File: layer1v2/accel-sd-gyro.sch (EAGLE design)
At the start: 17 parts, among them IC2 LGD20H, U1 MMA8452Q, U2 microSD

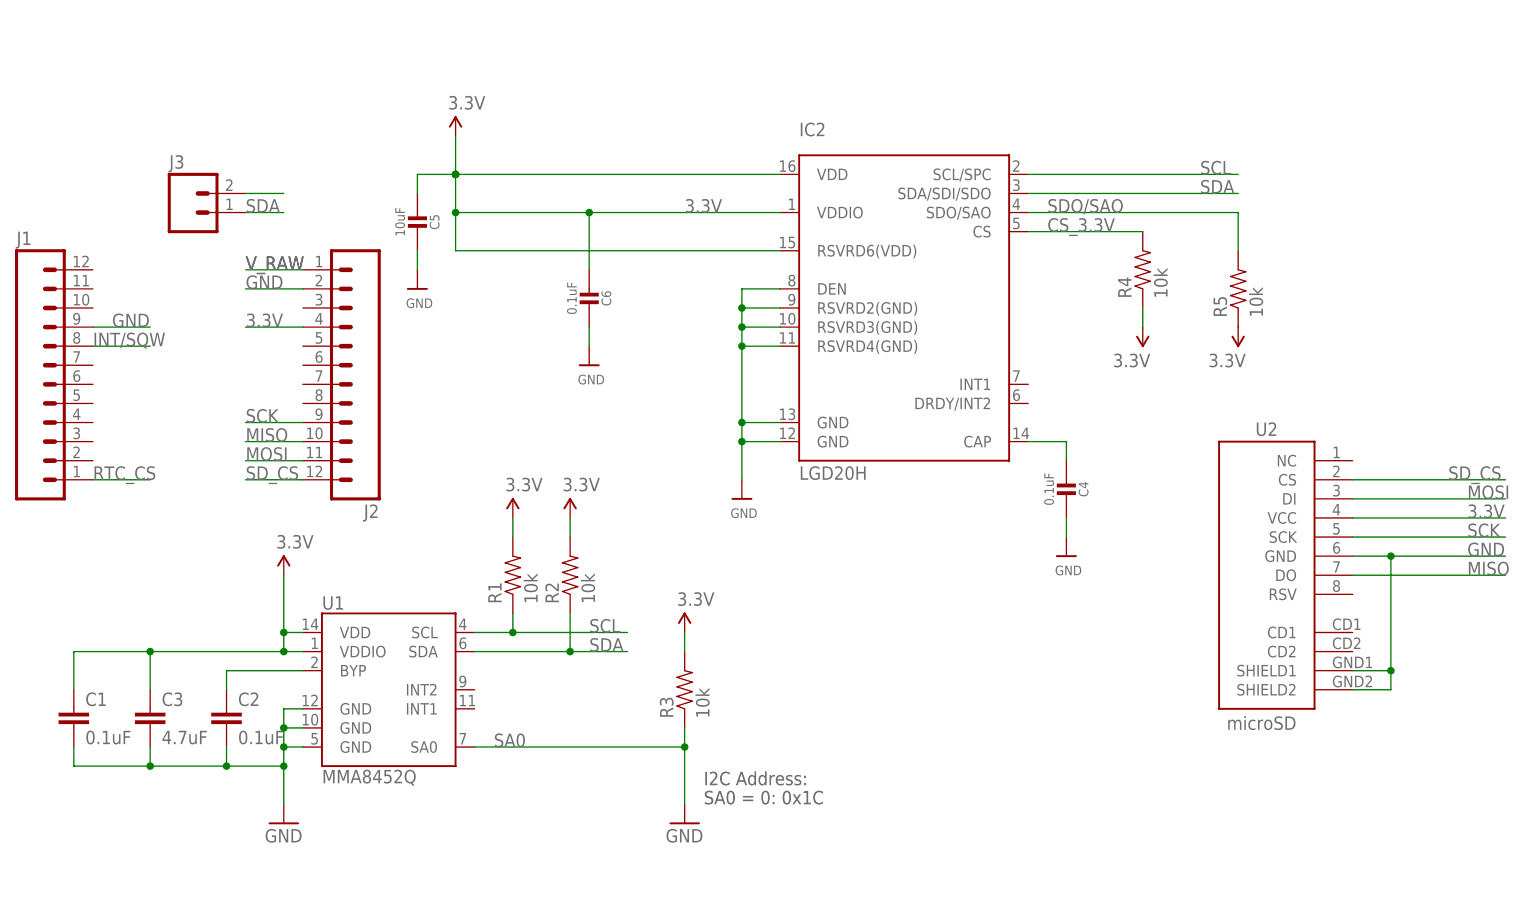
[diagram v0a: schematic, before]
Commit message: intial layout of v2 board, consldated i2c resisor, added header pin row
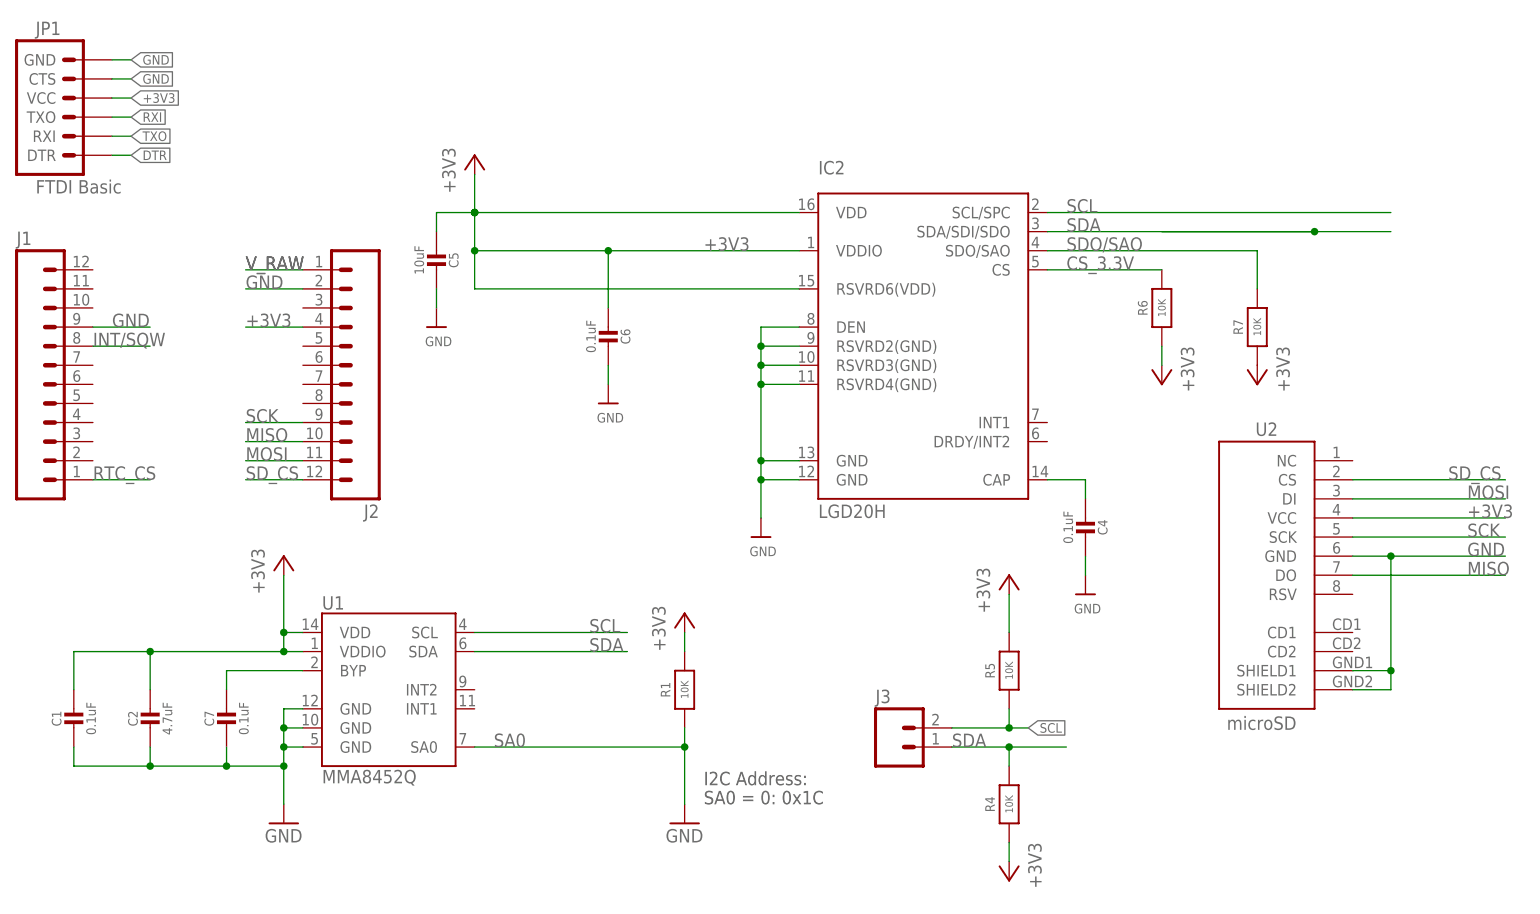
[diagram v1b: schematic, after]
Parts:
- removed C3: 4.7uF, SparkFun:CAP0402-CAP
- removed R2, R3: 10k, SparkFun:RESISTOR0402-RES
- added C7: 0.1uF, microbuilder:CAP_CERAMIC0805-NOOUTLINE
- added JP1: FTDI Basic, SparkFun:ARDUINO_SERIAL_PROGRAMPTH
- added R6: 10K, microbuilder:RESISTOR_0805MP
- added R7: 10K, microbuilder:RESISTOR0805_NOOUTLINE
- C1: device SparkFun:CAP0402-CAP -> microbuilder:CAP_CERAMIC0805-NOOUTLINE
- C2: value 0.1uF -> 4.7uF; device SparkFun:CAP0402-CAP -> microbuilder:CAP_CERAMIC0805-NOOUTLINE
- R1: value 10k -> 10K; device SparkFun:RESISTOR0402-RES -> microbuilder:RESISTOR_0805MP
- R4, R5: value 10k -> 10K; device SparkFun:RESISTOR0402-RES -> microbuilder:RESISTOR0805_NOOUTLINE
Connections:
- removed net 3.3V: C1.1, C3.1, C5.2, C6.2, IC2.RSVRD6(VDD), IC2.VDD, IC2.VDDIO, J2.4, R1.2, R2.2, R3.2, R4.1, R5.1, U1.VDD, U1.VDDIO, U2.VCC
- new net +3V3: C1.1, C2.1, C5.2, C6.2, IC2.RSVRD6(VDD), IC2.VDD, IC2.VDDIO, J2.4, JP1.VCC, R1.2, R4.1, R5.2, R6.1, R7.1, U1.VDD, U1.VDDIO, U2.VCC
- new net DTR: JP1.DTR
- new net RXI: JP1.TXO
- new net TXO: JP1.RXI
- net BYP: now also C7.1; no longer C2.1
- net CS_3.3V: now also R6.2; no longer R4.2
- net GND: now also C7.2, JP1.CTS, JP1.GND; no longer C3.2
- net SA0: now also R1.1; no longer R3.1
- net SCL: now also R5.1; no longer R1.1
- net SDA: now also R4.2; no longer R2.1
- net SDO/SAO: now also R7.2; no longer R5.2
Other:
- moved on the sheet: C2, C4, C5, C6, IC2, J3

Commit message: layer 1 tweaks and silk
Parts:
- removed JP1: FTDI Basic, SparkFun:ARDUINO_SERIAL_PROGRAMPTH
- removed R6: 10K, microbuilder:RESISTOR_0805MP
- removed R7: 10K, microbuilder:RESISTOR0805_NOOUTLINE
- added R2: 10K, microbuilder:RESISTOR0805_NOOUTLINE
- added R3: 10K, microbuilder:RESISTOR_0805MP
- R1: device microbuilder:RESISTOR_0805MP -> microbuilder:RESISTOR0805_NOOUTLINE
- R4: device microbuilder:RESISTOR0805_NOOUTLINE -> microbuilder:RESISTOR_0805MP
- renumbered C7 to C3
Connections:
- removed net DTR: JP1.DTR
- removed net RXI: JP1.TXO
- removed net TXO: JP1.RXI
- net +3V3: now also R2.1, R3.2, R5.1; no longer JP1.VCC, R5.2, R6.1, R7.1
- net CS_3.3V: now also R4.2; no longer R6.2
- net GND: no longer JP1.CTS, JP1.GND
- net SA0: now also R3.1; no longer R1.1
- net SCL: now also R1.1; no longer R5.1
- net SDA: now also R2.2; no longer R4.2
- net SDO/SAO: now also R5.2; no longer R7.2
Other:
- moved on the sheet: R1, R4, R5
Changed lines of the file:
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@@
 <part name="C6" library="microbuilder" deviceset="CAP_CERAMIC" device="0805-NOOUTLINE" value="0.1uF"/>
 <part name="U$7" library="microbuilder" deviceset="GND" device=""/>
-<part name="R4" library="microbuilder" deviceset="RESISTOR" device="0805_NOOUTLINE" value="10K"/>
-<part name="R5" library="microbuilder" deviceset="RESISTOR" device="0805_NOOUTLINE" value="10K"/>
+<part name="R2" library="microbuilder" deviceset="RESISTOR" device="0805_NOOUTLINE" value="10K"/>
+<part name="R1" library="microbuilder" deviceset="RESISTOR" device="0805_NOOUTLINE" value="10K"/>
 <part name="+3V4" library="supply1" deviceset="+3V3" device=""/>
 <part name="+3V5" library="supply1" deviceset="+3V3" device=""/>
-<part name="R6" library="microbuilder" deviceset="RESISTOR" device="_0805MP" value="10K"/>
+<part name="R4" library="microbuilder" deviceset="RESISTOR" device="_0805MP" value="10K"/>
 <part name="+3V1" library="supply1" deviceset="+3V3" device=""/>
 <part name="+3V7" library="supply1" deviceset="+3V3" device=""/>
-<part name="R7" library="microbuilder" deviceset="RESISTOR" device="0805_NOOUTLINE" value="10K"/>
+<part name="R5" library="microbuilder" deviceset="RESISTOR" device="0805_NOOUTLINE" value="10K"/>
 <part name="+3V9" library="supply1" deviceset="+3V3" device=""/>
 <part name="IC2" library="microbuilder" deviceset="GYRO_L3GD20H" device="" value="LGD20H"/>
@@
 <part name="+3V2" library="supply1" deviceset="+3V3" device=""/>
 <part name="+3V3" library="supply1" deviceset="+3V3" device=""/>
-<part name="R1" library="microbuilder" deviceset="RESISTOR" device="_0805MP" value="10K"/>
-<part name="JP1" library="SparkFun" deviceset="ARDUINO_SERIAL_PROGRAM" device="PTH" value="FTDI Basic"/>
-<part name="C7" library="microbuilder" deviceset="CAP_CERAMIC" device="0805-NOOUTLINE" value="0.1uF"/>
+<part name="R3" library="microbuilder" deviceset="RESISTOR" device="_0805MP" value="10K"/>
+<part name="C3" library="microbuilder" deviceset="CAP_CERAMIC" device="0805-NOOUTLINE" value="0.1uF"/>
 <part name="C1" library="microbuilder" deviceset="CAP_CERAMIC" device="0805-NOOUTLINE" value="0.1uF"/>
 <part name="C2" library="microbuilder" deviceset="CAP_CERAMIC" device="0805-NOOUTLINE" value="4.7uF"/>
@@
 <instance part="C6" gate="G$1" x="81.28" y="68.58" rot="R180"/>
 <instance part="U$7" gate="G$1" x="81.28" y="58.42"/>
-<instance part="R4" gate="G$1" x="134.62" y="5.08" rot="R90"/>
-<instance part="R5" gate="G$1" x="134.62" y="22.86" rot="R90"/>
+<instance part="R2" gate="G$1" x="134.62" y="5.08" rot="R90"/>
+<instance part="R1" gate="G$1" x="134.62" y="22.86" rot="R90"/>
 <instance part="+3V4" gate="G$1" x="134.62" y="35.56"/>
 <instance part="+3V5" gate="G$1" x="134.62" y="-5.08" rot="R180"/>
-<instance part="R6" gate="G$1" x="154.94" y="71.12" rot="R90"/>
+<instance part="R4" gate="G$1" x="154.94" y="71.12" rot="R90"/>
 <instance part="+3V1" gate="G$1" x="154.94" y="60.96" rot="R180"/>
 <instance part="+3V7" gate="G$1" x="63.5" y="91.44"/>
-<instance part="R7" gate="G$1" x="167.64" y="68.58" rot="R90"/>
+<instance part="R5" gate="G$1" x="167.64" y="68.58" rot="R90"/>
 <instance part="+3V9" gate="G$1" x="167.64" y="60.96" rot="R180"/>
 <instance part="IC2" gate="G$1" x="124.46" y="66.04"/>
@@
 <instance part="+3V2" gate="G$1" x="38.1" y="38.1"/>
 <instance part="+3V3" gate="G$1" x="91.44" y="30.48"/>
-<instance part="R1" gate="G$1" x="91.44" y="20.32" rot="R90"/>
-<instance part="JP1" gate="G$1" x="10.16" y="96.52"/>
-<instance part="C7" gate="G$1" x="30.48" y="15.24"/>
+<instance part="R3" gate="G$1" x="91.44" y="20.32" rot="R90"/>
+<instance part="C3" gate="G$1" x="30.48" y="15.24"/>
 <instance part="C1" gate="G$1" x="10.16" y="15.24"/>
 <instance part="C2" gate="G$1" x="20.32" y="15.24"/>
@@
 <wire x1="30.48" y1="22.86" x2="30.48" y2="20.32" width="0.1524" layer="91"/>
 <pinref part="U1" gate="G$1" pin="BYP"/>
-<pinref part="C7" gate="G$1" pin="1"/>
+<pinref part="C3" gate="G$1" pin="1"/>
 </segment>
 </net>
@@
 <pinref part="U1" gate="G$1" pin="GND@1"/>
 <pinref part="U1" gate="G$1" pin="GND@2"/>
-<pinref part="C7" gate="G$1" pin="2"/>
+<pinref part="C3" gate="G$1" pin="2"/>
 <pinref part="C1" gate="G$1" pin="2"/>
 <pinref part="C2" gate="G$1" pin="2"/>
@@
 <pinref part="U$7" gate="G$1" pin="GND"/>
 </segment>
-<segment>
-<wire x1="15.24" y1="101.6" x2="17.78" y2="101.6" width="0.1524" layer="91"/>
-<pinref part="JP1" gate="G$1" pin="CTS"/>
-<label x="17.78" y="101.6" size="1.27" layer="95" xref="yes"/>
-</segment>
-<segment>
-<wire x1="15.24" y1="104.14" x2="17.78" y2="104.14" width="0.1524" layer="91"/>
-<pinref part="JP1" gate="G$1" pin="GND"/>
-<label x="17.78" y="104.14" size="1.27" layer="95" xref="yes"/>
-</segment>
 </net>
 <net name="SCL" class="0">
@@
 <wire x1="127" y1="15.24" x2="134.62" y2="15.24" width="0.1524" layer="91"/>
 <label x="137.16" y="15.24" size="1.27" layer="95" xref="yes"/>
-<pinref part="R5" gate="G$1" pin="1"/>
+<pinref part="R1" gate="G$1" pin="1"/>
 <wire x1="134.62" y1="15.24" x2="137.16" y2="15.24" width="0.1524" layer="91"/>
 <wire x1="134.62" y1="15.24" x2="134.62" y2="17.78" width="0.1524" layer="91"/>
@@
 <wire x1="127" y1="12.7" x2="134.62" y2="12.7" width="0.1524" layer="91"/>
 <label x="127" y="12.7" size="1.778" layer="95"/>
-<pinref part="R4" gate="G$1" pin="2"/>
+<pinref part="R2" gate="G$1" pin="2"/>
 <wire x1="134.62" y1="12.7" x2="142.24" y2="12.7" width="0.1524" layer="91"/>
 <wire x1="134.62" y1="10.16" x2="134.62" y2="12.7" width="0.1524" layer="91"/>
@@
 <pinref part="U1" gate="G$1" pin="SA0"/>
 <pinref part="GND2" gate="1" pin="GND"/>
-<pinref part="R1" gate="G$1" pin="1"/>
+<pinref part="R3" gate="G$1" pin="1"/>
 </segment>
 </net>
@@
 <wire x1="167.64" y1="78.74" x2="167.64" y2="73.66" width="0.1524" layer="91"/>
 <label x="142.24" y="78.74" size="1.778" layer="95"/>
-<pinref part="R7" gate="G$1" pin="2"/>
+<pinref part="R5" gate="G$1" pin="2"/>
 <pinref part="IC2" gate="G$1" pin="SDO/SAO"/>
 </segment>
@@
 <segment>
 <wire x1="134.62" y1="33.02" x2="134.62" y2="27.94" width="0.1524" layer="91"/>
-<pinref part="R5" gate="G$1" pin="2"/>
+<pinref part="R1" gate="G$1" pin="2"/>
 <pinref part="+3V4" gate="G$1" pin="+3V3"/>
 </segment>
 <segment>
 <wire x1="134.62" y1="-2.54" x2="134.62" y2="0" width="0.1524" layer="91"/>
+<pinref part="R2" gate="G$1" pin="1"/>
+<pinref part="+3V5" gate="G$1" pin="+3V3"/>
+</segment>
+<segment>
+<wire x1="154.94" y1="63.5" x2="154.94" y2="66.04" width="0.1524" layer="91"/>
 <pinref part="R4" gate="G$1" pin="1"/>
-<pinref part="+3V5" gate="G$1" pin="+3V3"/>
-</segment>
-<segment>
-<wire x1="154.94" y1="63.5" x2="154.94" y2="66.04" width="0.1524" layer="91"/>
-<pinref part="R6" gate="G$1" pin="1"/>
 <pinref part="+3V1" gate="G$1" pin="+3V3"/>
 </segment>
@@
 </segment>
 <segment>
-<pinref part="R7" gate="G$1" pin="1"/>
+<pinref part="R5" gate="G$1" pin="1"/>
 <pinref part="+3V9" gate="G$1" pin="+3V3"/>
 </segment>
@@
 <wire x1="91.44" y1="27.94" x2="91.44" y2="25.4" width="0.1524" layer="91"/>
 <pinref part="+3V3" gate="G$1" pin="+3V3"/>
-<pinref part="R1" gate="G$1" pin="2"/>
+<pinref part="R3" gate="G$1" pin="2"/>
 </segment>
 <segment>
@@
 <label x="195.58" y="43.18" size="1.778" layer="95"/>
 </segment>
-<segment>
-<wire x1="15.24" y1="99.06" x2="17.78" y2="99.06" width="0.1524" layer="91"/>
-<pinref part="JP1" gate="G$1" pin="VCC"/>
-<label x="17.78" y="99.06" size="1.27" layer="95" xref="yes"/>
-</segment>
 </net>
 <net name="CS_3.3V" class="0">
@@
 <wire x1="139.7" y1="76.2" x2="154.94" y2="76.2" width="0.1524" layer="91"/>
 <label x="142.24" y="76.2" size="1.778" layer="95"/>
-<pinref part="R6" gate="G$1" pin="2"/>
+<pinref part="R4" gate="G$1" pin="2"/>
 <pinref part="IC2" gate="G$1" pin="CS"/>
 </segment>
 </net>
-<net name="TXO" class="0">
-<segment>
-<wire x1="15.24" y1="93.98" x2="17.78" y2="93.98" width="0.1524" layer="91"/>
-<pinref part="JP1" gate="G$1" pin="RXI"/>
-<label x="17.78" y="93.98" size="1.27" layer="95" xref="yes"/>
-</segment>
-</net>
-<net name="DTR" class="0">
-<segment>
-<wire x1="15.24" y1="91.44" x2="17.78" y2="91.44" width="0.1524" layer="91"/>
-<pinref part="JP1" gate="G$1" pin="DTR"/>
-<label x="17.78" y="91.44" size="1.27" layer="95" xref="yes"/>
-</segment>
-</net>
-<net name="RXI" class="0">
-<segment>
-<wire x1="15.24" y1="96.52" x2="17.78" y2="96.52" width="0.1524" layer="91"/>
-<pinref part="JP1" gate="G$1" pin="TXO"/>
-<label x="17.78" y="96.52" size="1.27" layer="95" xref="yes"/>
-</segment>
-</net>

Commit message: silk screen
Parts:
- R4: device microbuilder:RESISTOR_0805MP -> microbuilder:RESISTOR0805_NOOUTLINE
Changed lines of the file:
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@@
 <part name="+3V4" library="supply1" deviceset="+3V3" device=""/>
 <part name="+3V5" library="supply1" deviceset="+3V3" device=""/>
-<part name="R4" library="microbuilder" deviceset="RESISTOR" device="_0805MP" value="10K"/>
 <part name="+3V1" library="supply1" deviceset="+3V3" device=""/>
 <part name="+3V7" library="supply1" deviceset="+3V3" device=""/>
@@
 <part name="C1" library="microbuilder" deviceset="CAP_CERAMIC" device="0805-NOOUTLINE" value="0.1uF"/>
 <part name="C2" library="microbuilder" deviceset="CAP_CERAMIC" device="0805-NOOUTLINE" value="4.7uF"/>
+<part name="R4" library="microbuilder" deviceset="RESISTOR" device="0805_NOOUTLINE" value="10K"/>
 </parts>
 <sheets>
@@
 <instance part="+3V4" gate="G$1" x="134.62" y="35.56"/>
 <instance part="+3V5" gate="G$1" x="134.62" y="-5.08" rot="R180"/>
-<instance part="R4" gate="G$1" x="154.94" y="71.12" rot="R90"/>
 <instance part="+3V1" gate="G$1" x="154.94" y="60.96" rot="R180"/>
 <instance part="+3V7" gate="G$1" x="63.5" y="91.44"/>
@@
 <instance part="C1" gate="G$1" x="10.16" y="15.24"/>
 <instance part="C2" gate="G$1" x="20.32" y="15.24"/>
+<instance part="R4" gate="G$1" x="154.94" y="71.12" rot="R90"/>
 </instances>
 <busses>
@@
 <segment>
 <wire x1="154.94" y1="63.5" x2="154.94" y2="66.04" width="0.1524" layer="91"/>
+<pinref part="+3V1" gate="G$1" pin="+3V3"/>
 <pinref part="R4" gate="G$1" pin="1"/>
-<pinref part="+3V1" gate="G$1" pin="+3V3"/>
 </segment>
 <segment>
@@
 <wire x1="139.7" y1="76.2" x2="154.94" y2="76.2" width="0.1524" layer="91"/>
 <label x="142.24" y="76.2" size="1.778" layer="95"/>
+<pinref part="IC2" gate="G$1" pin="CS"/>
 <pinref part="R4" gate="G$1" pin="2"/>
-<pinref part="IC2" gate="G$1" pin="CS"/>
-</segment>
-</net>
+</segment>
+</net>

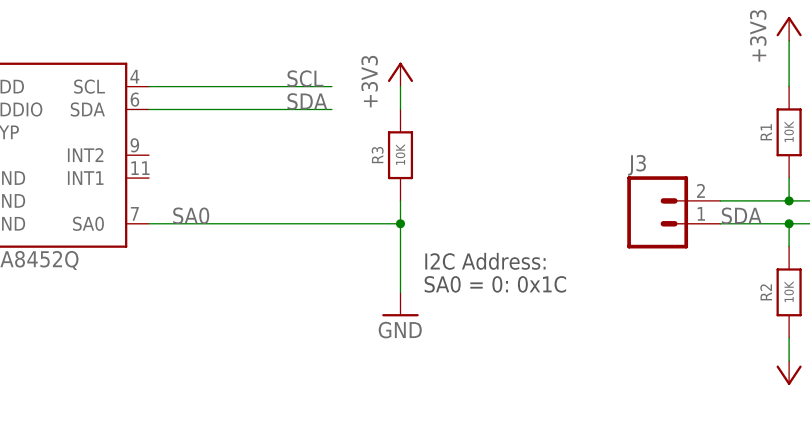
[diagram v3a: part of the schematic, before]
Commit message: tweacked sd traces
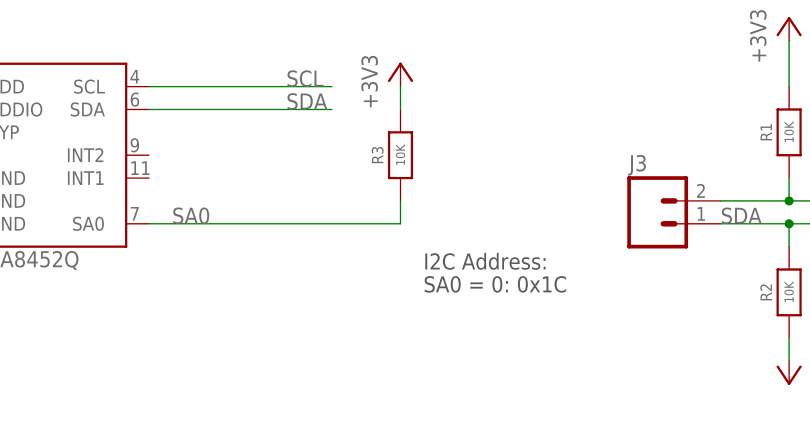
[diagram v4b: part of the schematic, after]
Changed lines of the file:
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@@
 <part name="U1" library="SparkFun" deviceset="MMA8452Q" device=""/>
 <part name="GND1" library="SparkFun" deviceset="GND" device=""/>
-<part name="GND2" library="SparkFun" deviceset="GND" device=""/>
 <part name="U2" library="SparkFun" deviceset="USD-SOCKET" device="SMD" value="microSD"/>
 <part name="J1" library="SparkFun-Connectors" deviceset="M12" device="PTH"/>
@@
 <instance part="U1" gate="G$1" x="50.8" y="20.32"/>
 <instance part="GND1" gate="1" x="38.1" y="2.54"/>
-<instance part="GND2" gate="1" x="91.44" y="2.54"/>
 <instance part="U2" gate="G$1" x="172.72" y="38.1" smashed="yes" rot="MR0">
 <attribute name="NAME" x="167.386" y="54.102" size="1.778" layer="95"/>
@@
 <segment>
 <wire x1="63.5" y1="12.7" x2="91.44" y2="12.7" width="0.1524" layer="91"/>
-<wire x1="91.44" y1="5.08" x2="91.44" y2="12.7" width="0.1524" layer="91"/>
 <wire x1="91.44" y1="12.7" x2="91.44" y2="15.24" width="0.1524" layer="91"/>
-<junction x="91.44" y="12.7"/>
 <label x="66.04" y="12.7" size="1.778" layer="95"/>
 <pinref part="U1" gate="G$1" pin="SA0"/>
-<pinref part="GND2" gate="1" pin="GND"/>
 <pinref part="R3" gate="G$1" pin="1"/>
 </segment>
